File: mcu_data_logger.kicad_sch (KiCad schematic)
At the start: 25 parts, among them U1 24LC1025, U2 24LC1025, U3 DS1337S_, U4 ATMEGA328P-AU, Y1 32.768 kHz, Y2 16MHz

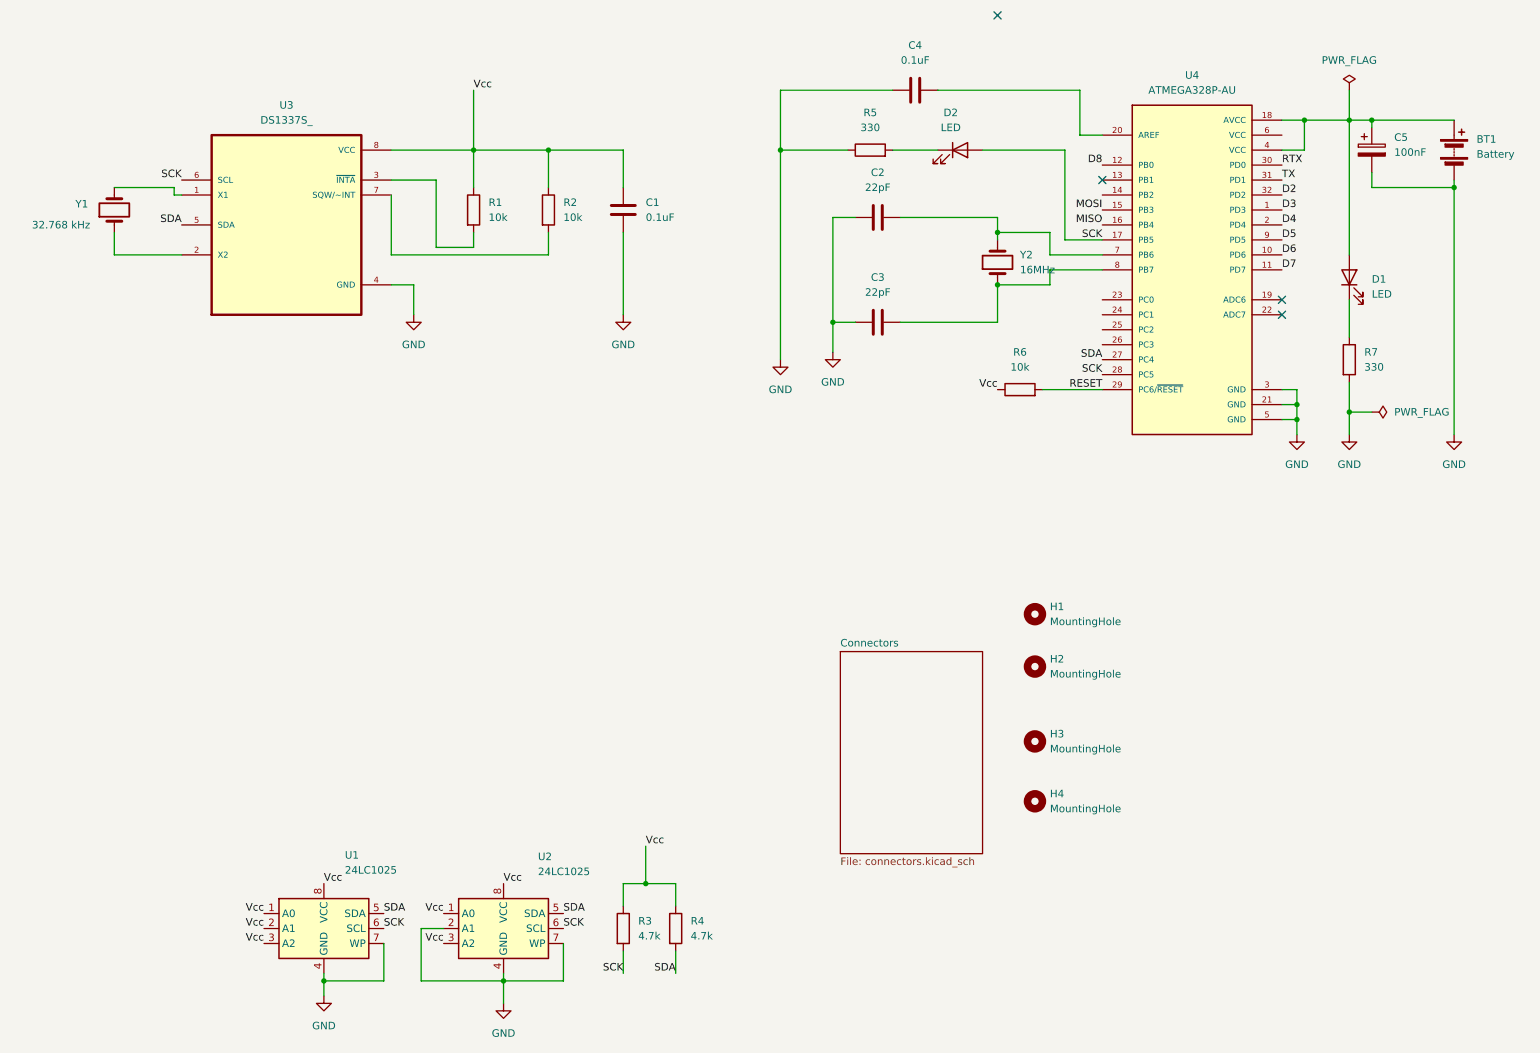
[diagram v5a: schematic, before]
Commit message: wiring for sheet 2 finished  and errors on the main sheet fixed
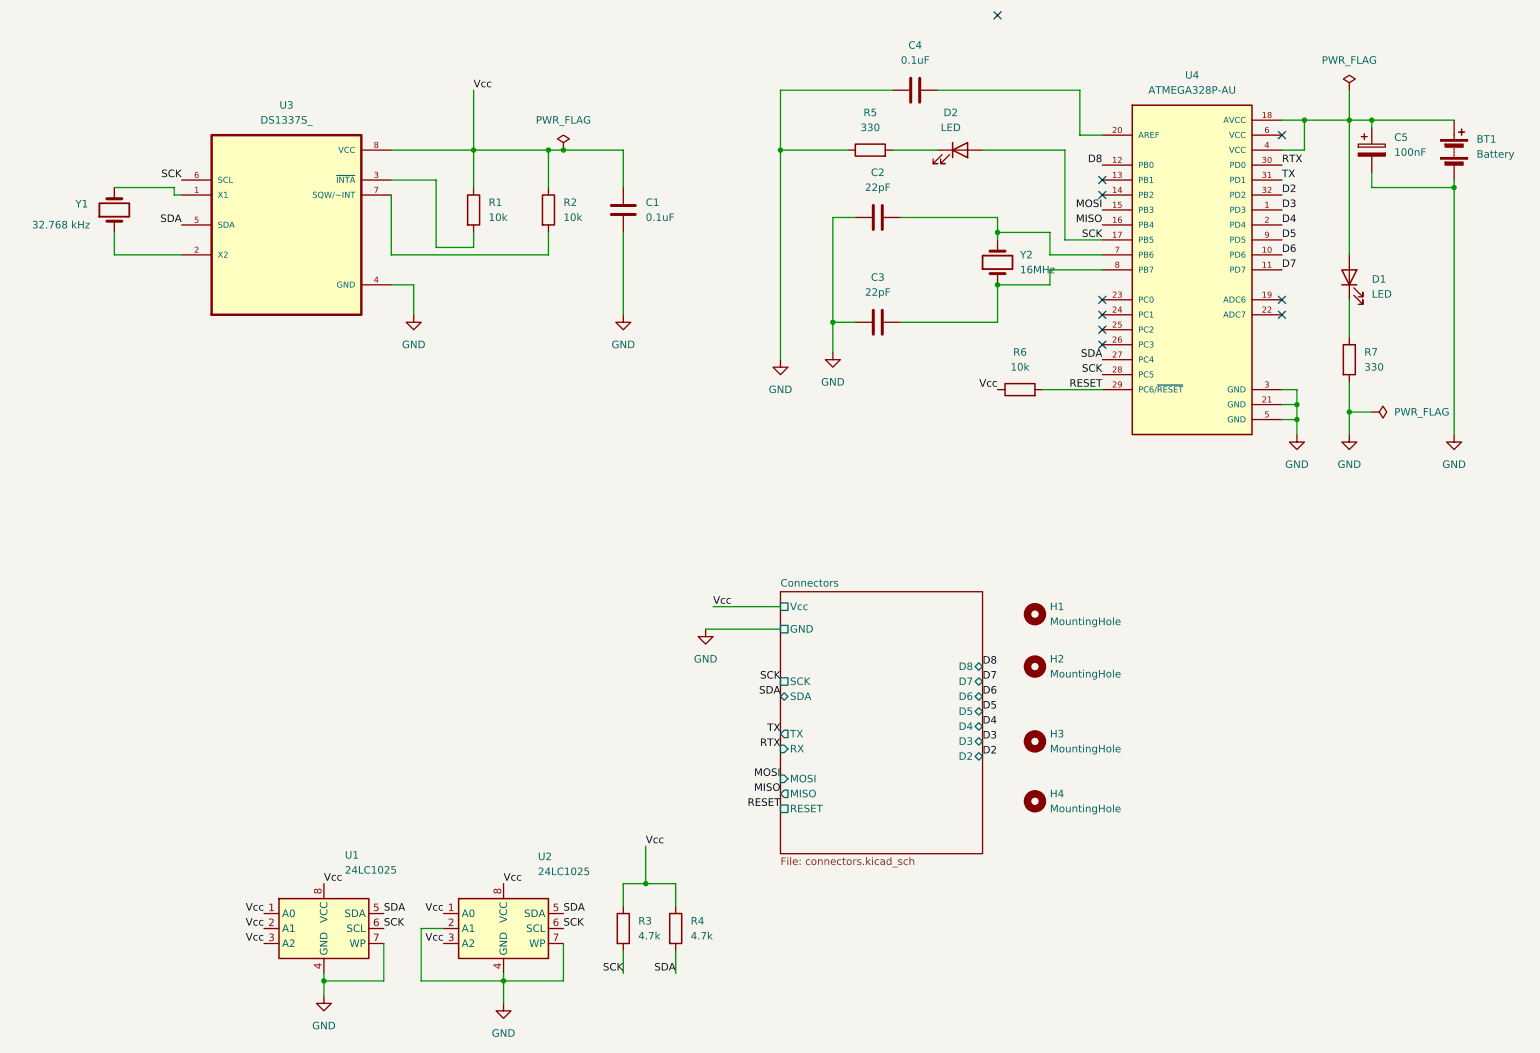
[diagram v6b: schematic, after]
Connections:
- no-connect marks 4 -> 10
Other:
- sheet Connectors ports: added D2, D3, D4, D5, D6, D7, D8, GND, MISO, MOSI, RESET, RX, SCK, SDA, TX, Vcc; removed none

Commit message: fixed references in sheet 2 to match the course material for the purpose of easier wiring during layout design stage
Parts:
- renumbered U3 to U2, U2 to U3
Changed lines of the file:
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@@
 		(on_board yes)
 		(dnp no)
-		(property "Reference" "U2"
+		(property "Reference" "U3"
 			(at 116.332 160.528 0)
 			(effects
@@
 			)
 		)
+		(property "Purpose" ""
+			(at 110.49 172.72 0)
+			(effects
+				(font
+					(size 1.27 1.27)
+				)
+			)
+		)
 		(pin "7"
 		)
@@
 			(project "mcu_data_logger"
 				(path "/8d241645-05dd-4180-8806-a9efe0716d11"
-					(reference "U2")
+					(reference "U3")
 					(unit 1)
 				)
@@
 		(dnp no)
 		(fields_autoplaced yes)
-		(property "Reference" "U3"
+		(property "Reference" "U2"
 			(at 73.66 33.02 0)
 			(effects
@@
 			)
 		)
+		(property "Purpose" ""
+			(at 73.66 53.34 0)
+			(effects
+				(font
+					(size 1.27 1.27)
+				)
+			)
+		)
 		(pin "5"
 		)
@@
 			(project ""
 				(path "/8d241645-05dd-4180-8806-a9efe0716d11"
-					(reference "U3")
-					(unit 1)
-				)
+					(reference "U2")
+					(unit 1)
+				)

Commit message: Added comments and graphics
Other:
- note added: "EEPROM"
- note added: "MCU"
- note added: "Mounting"
- note added: "Real Time Clock"
- moved on the sheet: H1, H2, H3, H4, R3, R4, U1, U3
